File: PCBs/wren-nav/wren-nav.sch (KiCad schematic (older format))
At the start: 90 parts, among them J1 TRRS_Jack, SW0 Reset, U1 Elite-C

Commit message: Quick nav update
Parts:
- U1: symbol wren-left-rescue:Elite-C-keebio -> wren-nav-rescue:Elite-C-keebio-wren-left-rescue
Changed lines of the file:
@@
 RIGHT
 $Comp
-L wren-left-rescue:Elite-C-keebio U1
+L wren-nav-rescue:Elite-C-keebio-wren-left-rescue U1
 U 1 1 6071F7CA
 P 2500 2000

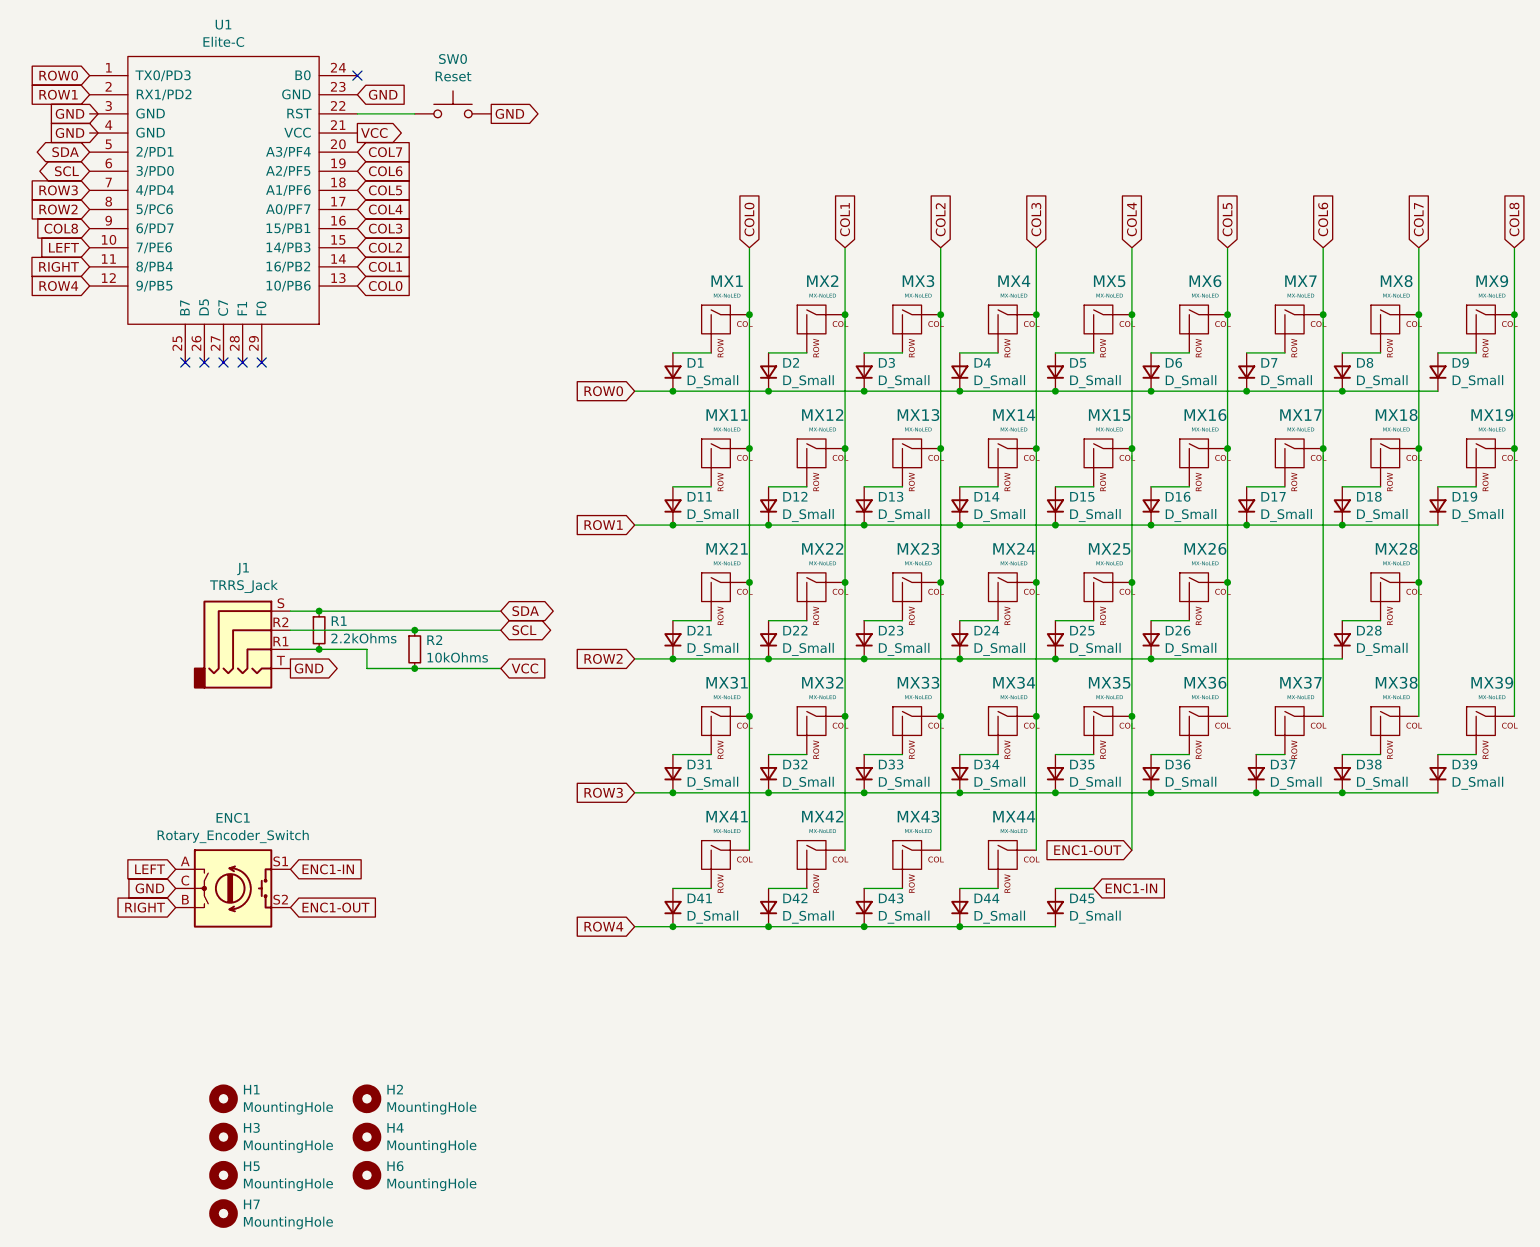
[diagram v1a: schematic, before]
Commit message: Standardize MCU Pins
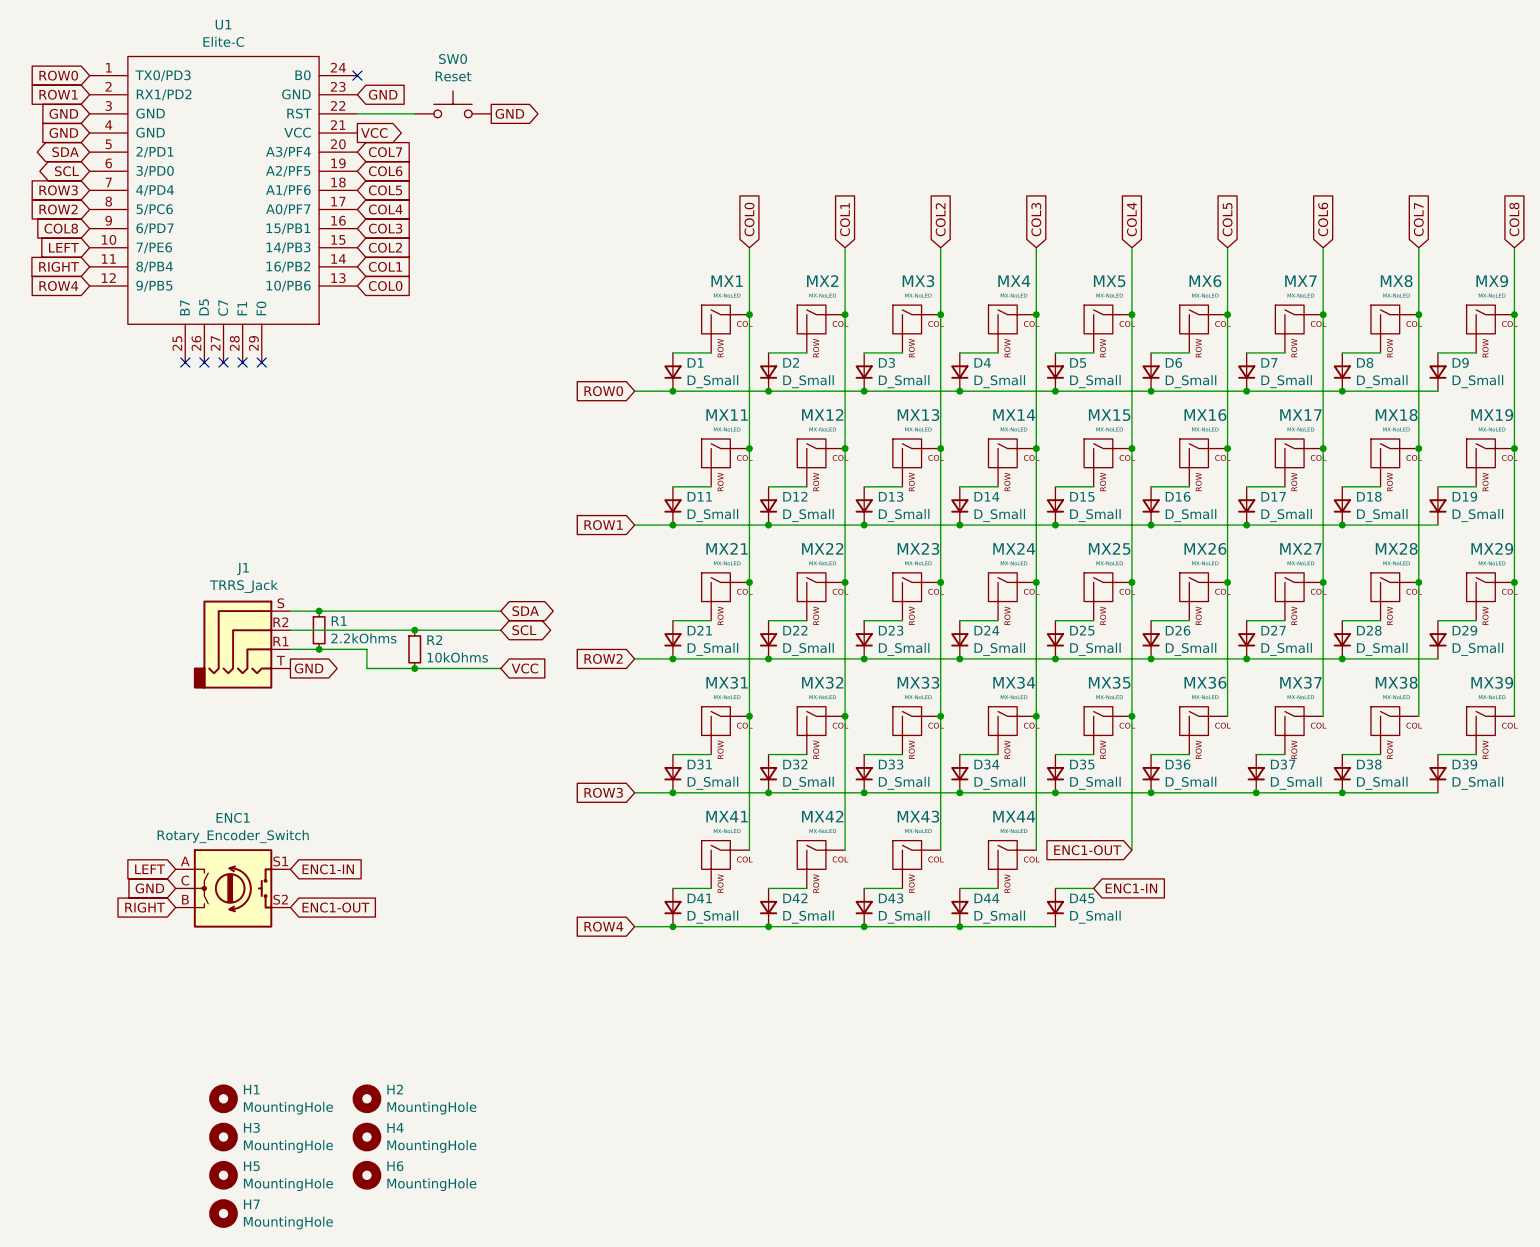
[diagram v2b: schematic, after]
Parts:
- added D27, D29: D_Small, footprints:D_SOD123_axial, symbol Device:D_Small
- added MX27, MX29: MX-NoLED, footprints:SW_MX_reversible, symbol MX_Alps_Hybrid:MX-NoLED
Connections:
- net COL6: now also MX27.1 (COL)
- net COL8: now also MX29.1 (COL)
- net GND: now also U1.3 (GND), U1.4 (GND)
- net ROW2: now also D27.1 (K), D29.1 (K)
- new net: D27.2 (A), MX27.2 (ROW)
- new net: D29.2 (A), MX29.2 (ROW)
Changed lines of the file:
@@
 Text GLabel 3950 4250 2    50   BiDi ~ 0
 SDA
-Text GLabel 1600 1650 2    50   Output ~ 0
-GND
-Text GLabel 1600 1750 2    50   Output ~ 0
-GND
 NoConn ~ 3200 1450
 NoConn ~ 2500 2950
@@
 	4850 5700 5050 5700
 Wire Wire Line
-	9250 3400 9250 4800
-Wire Wire Line
-	8250 3400 8250 4800
-Wire Wire Line
-	7350 4500 8350 4500
+	9250 3400 9250 4100
+Wire Wire Line
+	8250 3400 8250 4100
+Wire Wire Line
+	7350 4500 7850 4500
 NoConn ~ 2600 2950
 NoConn ~ 2700 2950
+$Comp
+L MX_Alps_Hybrid:MX-NoLED MX27
+U 1 1 6089828C
+P 8100 4150
+F 0 "MX27" H 8133 4373 60  0000 C CNN
+F 1 "MX-NoLED" H 8133 4299 20  0000 C CNN
+F 2 "footprints:SW_MX_reversible" H 7475 4125 60  0001 C CNN
+F 3 "" H 7475 4125 60  0001 C CNN
+	1    8100 4150
+	1    0    0    -1
+$EndComp
+Connection ~ 8250 4100
+Wire Wire Line
+	8250 4100 8250 4800
+$Comp
+L MX_Alps_Hybrid:MX-NoLED MX29
+U 1 1 60898948
+P 9100 4150
+F 0 "MX29" H 9133 4373 60  0000 C CNN
+F 1 "MX-NoLED" H 9133 4299 20  0000 C CNN
+F 2 "footprints:SW_MX_reversible" H 8475 4125 60  0001 C CNN
+F 3 "" H 8475 4125 60  0001 C CNN
+	1    9100 4150
+	1    0    0    -1
+$EndComp
+Connection ~ 9250 4100
+Wire Wire Line
+	9250 4100 9250 4800
+$Comp
+L Device:D_Small D27
+U 1 1 608993BF
+P 7850 4400
+F 0 "D27" V 7896 4330 50  0000 R CNN
+F 1 "D_Small" V 7805 4330 50  0000 R CNN
+F 2 "footprints:D_SOD123_axial" V 7850 4400 50  0001 C CNN
+F 3 "~" V 7850 4400 50  0001 C CNN
+	1    7850 4400
+	0    -1   -1   0
+$EndComp
+Connection ~ 7850 4500
+Wire Wire Line
+	7850 4500 8350 4500
+$Comp
+L Device:D_Small D29
+U 1 1 608998FA
+P 8850 4400
+F 0 "D29" V 8896 4330 50  0000 R CNN
+F 1 "D_Small" V 8805 4330 50  0000 R CNN
+F 2 "footprints:D_SOD123_axial" V 8850 4400 50  0001 C CNN
+F 3 "~" V 8850 4400 50  0001 C CNN
+	1    8850 4400
+	0    -1   -1   0
+$EndComp
+Wire Wire Line
+	7850 4300 8050 4300
+Wire Wire Line
+	8850 4300 9050 4300
+Wire Wire Line
+	8850 4500 8350 4500
+Connection ~ 8350 4500
+Text GLabel 1800 1650 0    50   Input ~ 0
+GND
+Text GLabel 1800 1750 0    50   Input ~ 0
+GND
 $EndSCHEMATC
